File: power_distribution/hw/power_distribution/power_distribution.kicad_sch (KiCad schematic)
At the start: 52 parts, among them J1 XT30-M_Ver, J2 JST-PH_01x02, J3 JST-PH_01x02, J4 JST-PH_01x02, Q1 60Vds, U1 LMR51635XFDDCR, U2 AP63205WU-7, U3 AP63203WU-7

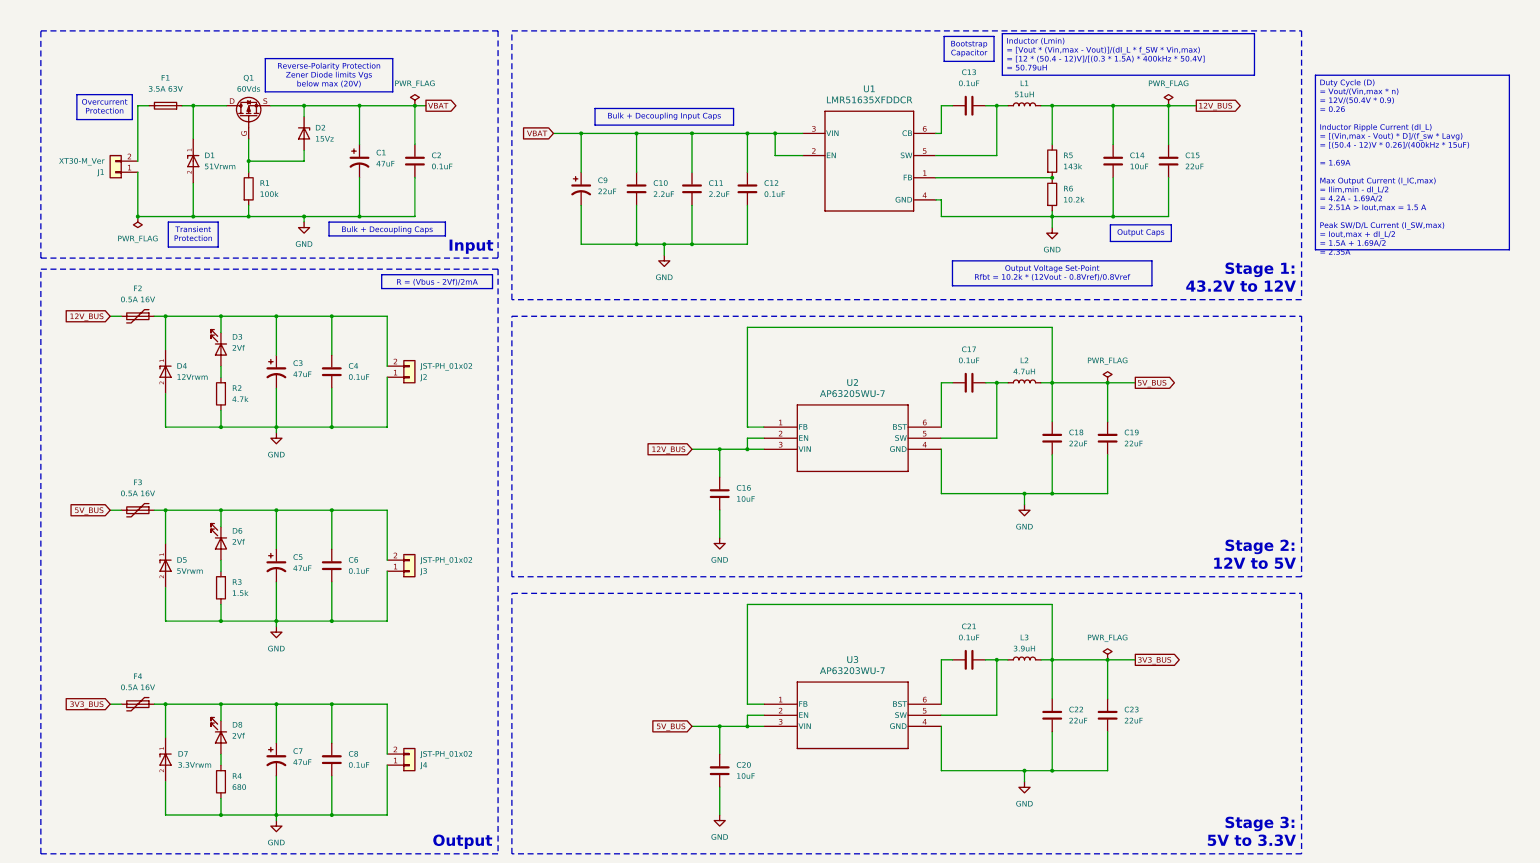
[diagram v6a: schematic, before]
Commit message: Flip LEDs and change RES symbols
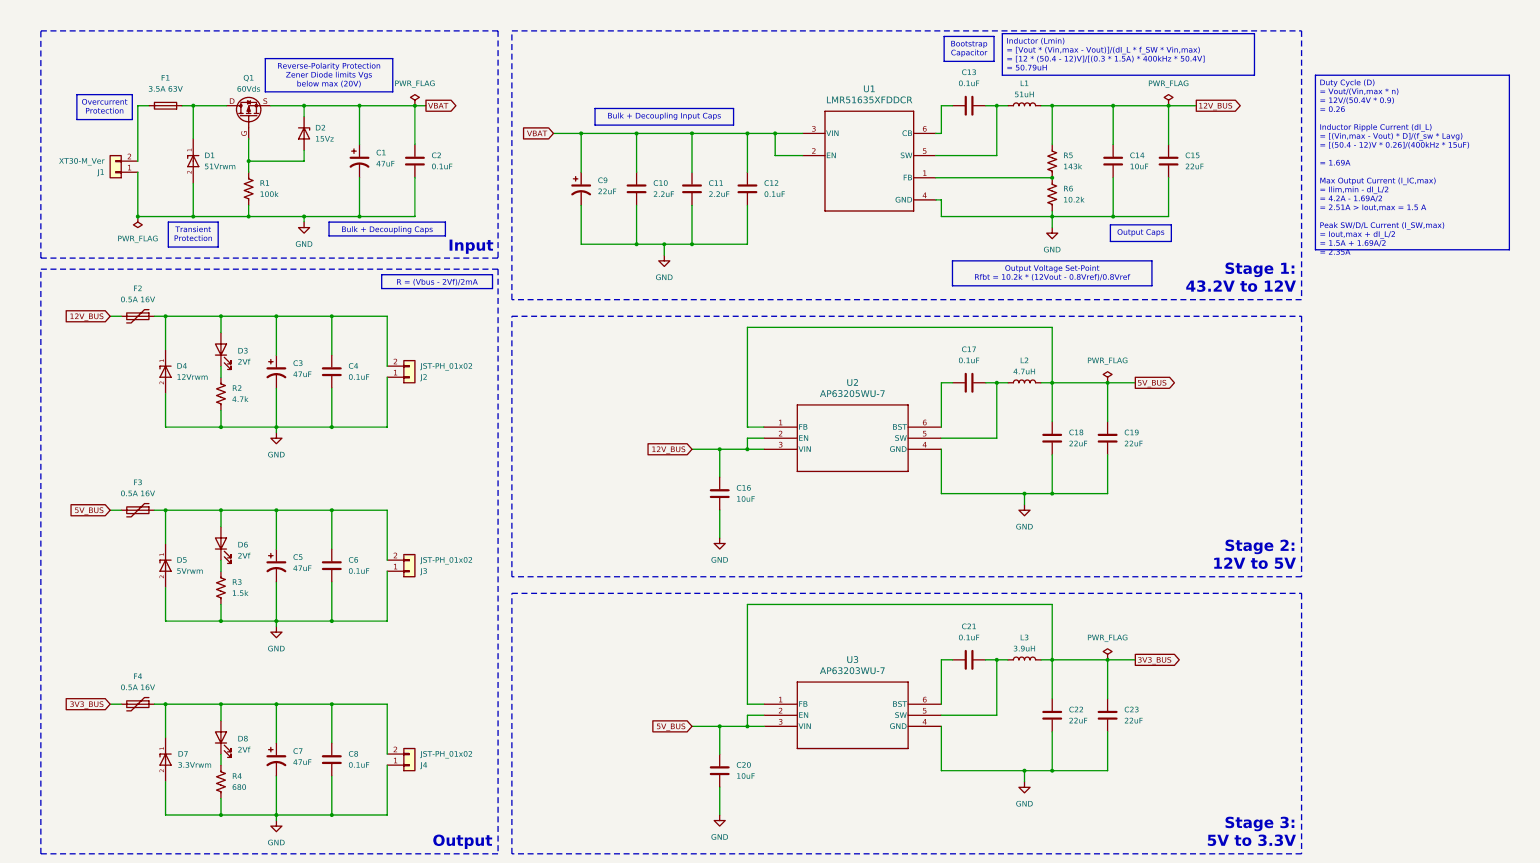
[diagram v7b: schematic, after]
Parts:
- R1, R2, R3, R4, R5, R6: symbol Device:R -> Device:R_US
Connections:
- net at C3.1, C4.1, D4.1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: now also D3.2 (A); no longer D3.1 (K)
- net at C7.1, C8.1, D7.1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: now also D8.2 (A); no longer D8.1 (K)
- net at C5.1, C6.1, D5.1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: now also D6.2 (A); no longer D6.1 (K)
- net at R2.2: now also D3.1 (K); no longer D3.2 (A)
- net at R3.2: now also D6.1 (K); no longer D6.2 (A)
- net at R4.2: now also D8.1 (K); no longer D8.2 (A)
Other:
- moved on the sheet: D3, D6, D8
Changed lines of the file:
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@@
 	(symbol
 		(lib_id "Device:LED")
-		(at 63.5 93.98 270)
+		(at 63.5 93.98 90)
 		(unit 1)
 		(exclude_from_sim no)
@@
 		(fields_autoplaced yes)
 		(property "Reference" "D3"
-			(at 66.04 91.1224 90)
-			(effects
-				(font
-					(size 1.27 1.27)
-				)
-				(justify left)
+			(at 67.31 94.2974 90)
+			(effects
+				(font
+					(size 1.27 1.27)
+				)
+				(justify right)
 			)
 		)
 		(property "Value" "2Vf"
-			(at 66.04 93.6624 90)
-			(effects
-				(font
-					(size 1.27 1.27)
-				)
-				(justify left)
+			(at 67.31 96.8374 90)
+			(effects
+				(font
+					(size 1.27 1.27)
+				)
+				(justify right)
 			)
 		)
@@
 	)
 	(symbol
-		(lib_id "Device:R")
+		(lib_id "Device:R_US")
 		(at 63.5 148.59 180)
 		(unit 1)
@@
 		)
 		(property "Footprint" ""
-			(at 65.278 148.59 90)
+			(at 62.484 148.336 90)
 			(effects
 				(font
@@
 			)
 		)
-		(property "Description" "Resistor"
+		(property "Description" "Resistor, US symbol"
 			(at 63.5 148.59 0)
 			(effects
@@
 	)
 	(symbol
-		(lib_id "Device:R")
+		(lib_id "Device:R_US")
 		(at 69.85 57.15 0)
 		(unit 1)
@@
 		)
 		(property "Footprint" ""
-			(at 68.072 57.15 90)
+			(at 70.866 57.404 90)
 			(effects
 				(font
@@
 			)
 		)
-		(property "Description" "Resistor"
+		(property "Description" "Resistor, US symbol"
 			(at 69.85 57.15 0)
 			(effects
@@
 	)
 	(symbol
-		(lib_id "Device:R")
+		(lib_id "Device:R_US")
 		(at 254 58.42 0)
 		(unit 1)
@@
 		)
 		(property "Footprint" ""
-			(at 252.222 58.42 90)
+			(at 255.016 58.674 90)
 			(effects
 				(font
@@
 			)
 		)
-		(property "Description" "Resistor"
+		(property "Description" "Resistor, US symbol"
 			(at 254 58.42 0)
 			(effects
@@
 	)
 	(symbol
-		(lib_id "Device:R")
+		(lib_id "Device:R_US")
 		(at 63.5 193.04 180)
 		(unit 1)
@@
 		)
 		(property "Footprint" ""
-			(at 65.278 193.04 90)
+			(at 62.484 192.786 90)
 			(effects
 				(font
@@
 			)
 		)
-		(property "Description" "Resistor"
+		(property "Description" "Resistor, US symbol"
 			(at 63.5 193.04 0)
 			(effects
@@
 	)
 	(symbol
-		(lib_id "Device:R")
+		(lib_id "Device:R_US")
 		(at 63.5 104.14 180)
 		(unit 1)
@@
 		)
 		(property "Footprint" ""
-			(at 65.278 104.14 90)
+			(at 62.484 103.886 90)
 			(effects
 				(font
@@
 			)
 		)
-		(property "Description" "Resistor"
+		(property "Description" "Resistor, US symbol"
 			(at 63.5 104.14 0)
 			(effects
@@
 	)
 	(symbol
-		(lib_id "Device:R")
+		(lib_id "Device:R_US")
 		(at 254 50.8 0)
 		(unit 1)
@@
 		)
 		(property "Footprint" ""
-			(at 252.222 50.8 90)
+			(at 255.016 51.054 90)
 			(effects
 				(font
@@
 			)
 		)
-		(property "Description" "Resistor"
+		(property "Description" "Resistor, US symbol"
 			(at 254 50.8 0)
 			(effects
@@
 	(symbol
 		(lib_id "Device:LED")
-		(at 63.5 138.43 270)
+		(at 63.5 138.43 90)
 		(unit 1)
 		(exclude_from_sim no)
@@
 		(fields_autoplaced yes)
 		(property "Reference" "D6"
-			(at 66.04 135.5724 90)
-			(effects
-				(font
-					(size 1.27 1.27)
-				)
-				(justify left)
+			(at 67.31 138.7474 90)
+			(effects
+				(font
+					(size 1.27 1.27)
+				)
+				(justify right)
 			)
 		)
 		(property "Value" "2Vf"
-			(at 66.04 138.1124 90)
-			(effects
-				(font
-					(size 1.27 1.27)
-				)
-				(justify left)
+			(at 67.31 141.2874 90)
+			(effects
+				(font
+					(size 1.27 1.27)
+				)
+				(justify right)
 			)
 		)
@@
 	(symbol
 		(lib_id "Device:LED")
-		(at 63.5 182.88 270)
+		(at 63.5 182.88 90)
 		(unit 1)
 		(exclude_from_sim no)
@@
 		(fields_autoplaced yes)
 		(property "Reference" "D8"
-			(at 66.04 180.0224 90)
-			(effects
-				(font
-					(size 1.27 1.27)
-				)
-				(justify left)
+			(at 67.31 183.1974 90)
+			(effects
+				(font
+					(size 1.27 1.27)
+				)
+				(justify right)
 			)
 		)
 		(property "Value" "2Vf"
-			(at 66.04 182.5624 90)
-			(effects
-				(font
-					(size 1.27 1.27)
-				)
-				(justify left)
-			)
-		)
+			(at 67.31 185.7374 90)
+			(effects
+				(font
+					(size 1.27 1.27)
+				)
+				(justify right)
+			)
+		)
